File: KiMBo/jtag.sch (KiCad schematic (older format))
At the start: 9 parts, among them U1 OSD3358, Y2 AH-32.768KDZY-T, Y3 7A-24.000MAAJ-T

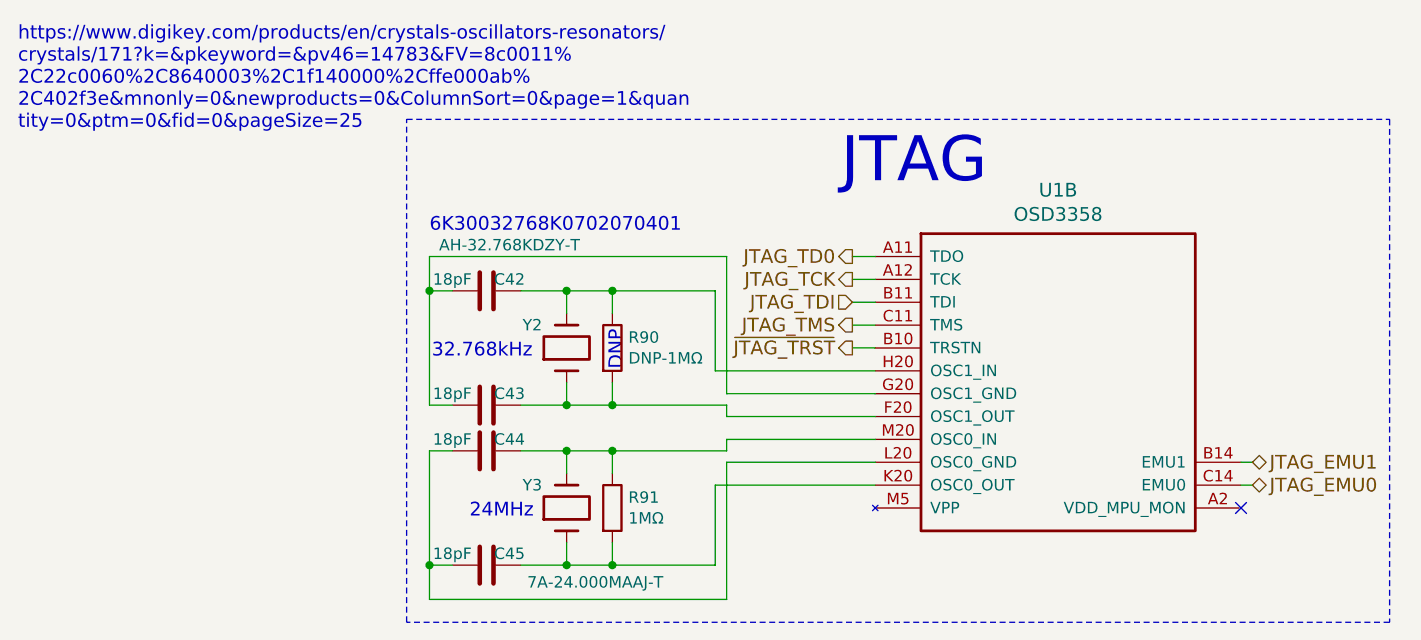
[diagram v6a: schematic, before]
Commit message: Add ferrite beads to the 5V and 3V pins at the SPI connectors
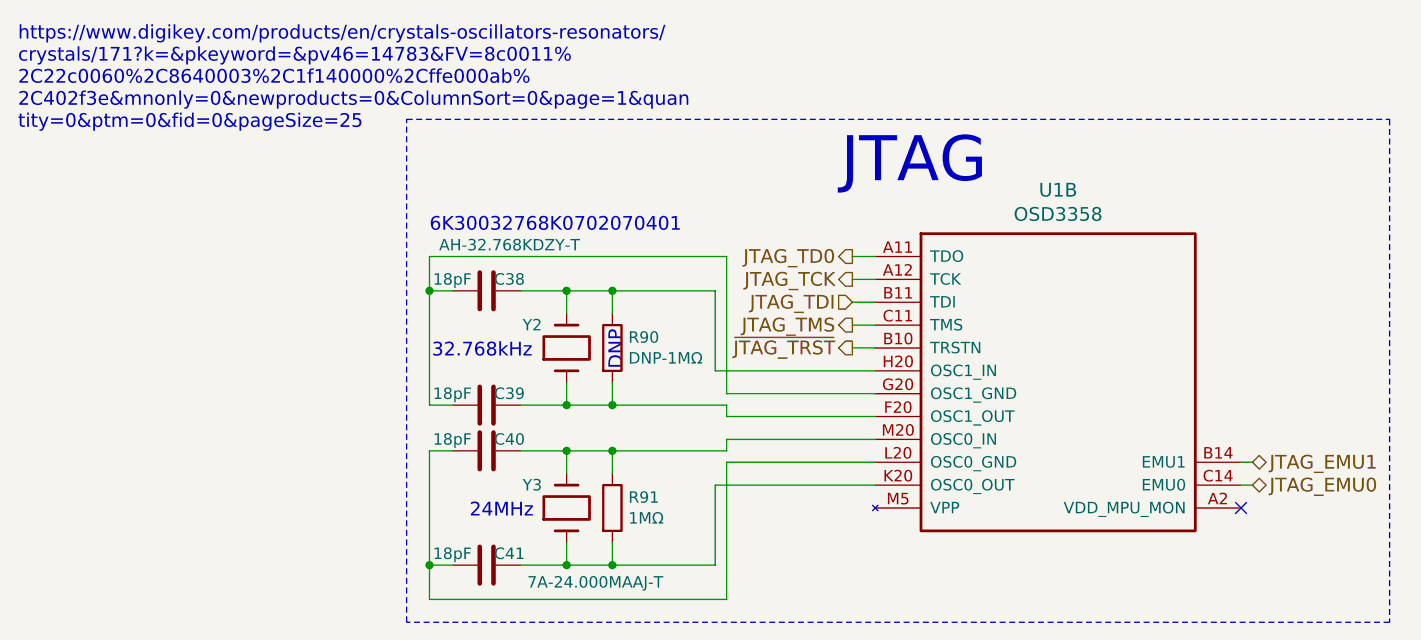
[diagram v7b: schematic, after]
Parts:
- renumbered C42 to C38, C43 to C39, C44 to C40, C45 to C41
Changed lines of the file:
@@
 $EndComp
 $Comp
-L C C44
+L C C40
 U 1 1 589C1D01
 P 4150 3750
-F 0 "C44" V 4200 3850 50  0000 C CNN
+F 0 "C40" V 4200 3850 50  0000 C CNN
 F 1 "18pF" V 4200 3600 50  0000 C CNN
 F 2 "Capacitors_SMD:C_0603" H 4150 3750 50  0001 C CNN
@@
 $EndComp
 $Comp
-L C C45
+L C C41
 U 1 1 589C1D08
 P 4150 4250
-F 0 "C45" V 4200 4350 50  0000 C CNN
+F 0 "C41" V 4200 4350 50  0000 C CNN
 F 1 "18pF" V 4200 4100 50  0000 C CNN
 F 2 "Capacitors_SMD:C_0603" H 4150 4250 50  0001 C CNN
@@
 $EndComp
 $Comp
-L C C43
+L C C39
 U 1 1 589C1D16
 P 4150 3550
-F 0 "C43" V 4200 3650 50  0000 C CNN
+F 0 "C39" V 4200 3650 50  0000 C CNN
 F 1 "18pF" V 4200 3400 50  0000 C CNN
 F 2 "Capacitors_SMD:C_0603" H 4150 3550 50  0001 C CNN
@@
 $EndComp
 $Comp
-L C C42
+L C C38
 U 1 1 589C1D1D
 P 4150 3050
-F 0 "C42" V 4200 3150 50  0000 C CNN
+F 0 "C38" V 4200 3150 50  0000 C CNN
 F 1 "18pF" V 4200 2900 50  0000 C CNN
 F 2 "Capacitors_SMD:C_0603" H 4150 3050 50  0001 C CNN

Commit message: Complete SPI, ADC, and Endstop header layout/position, add zone around the SiP
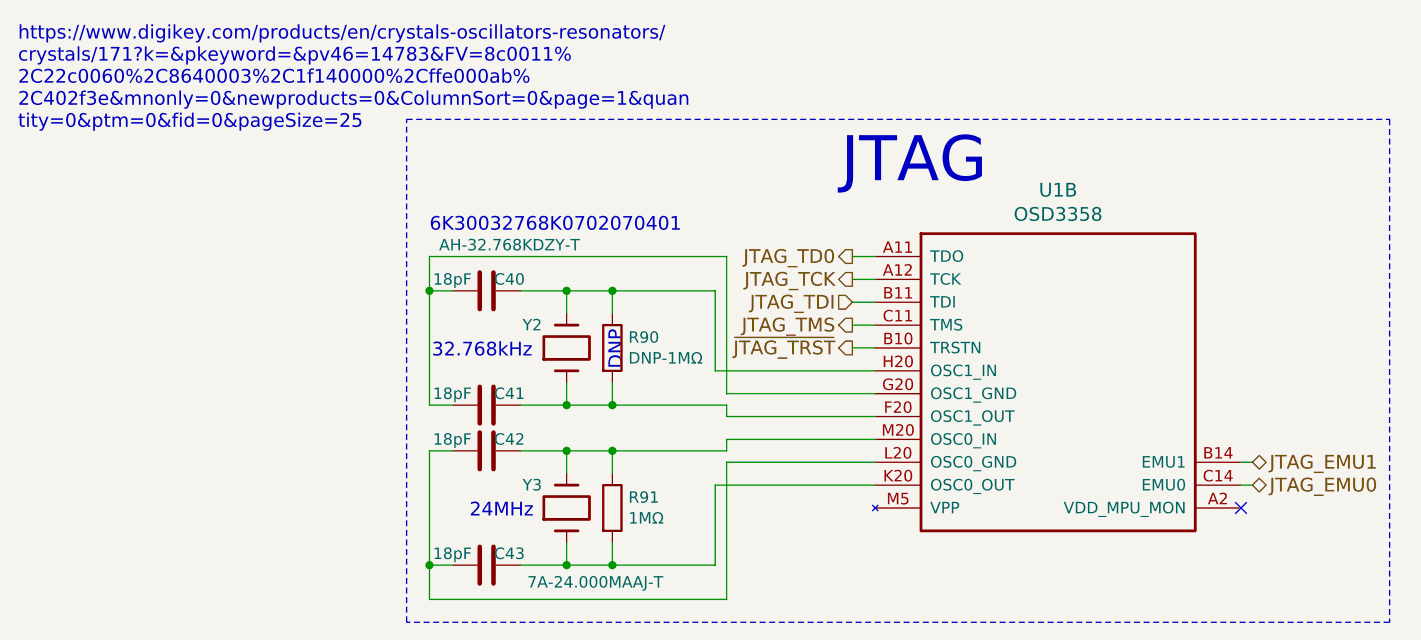
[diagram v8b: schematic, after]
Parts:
- renumbered C38 to C40, C39 to C41, C40 to C42, C41 to C43
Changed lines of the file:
@@
 $EndComp
 $Comp
-L C C40
+L C C42
 U 1 1 589C1D01
 P 4150 3750
-F 0 "C40" V 4200 3850 50  0000 C CNN
+F 0 "C42" V 4200 3850 50  0000 C CNN
 F 1 "18pF" V 4200 3600 50  0000 C CNN
 F 2 "Capacitors_SMD:C_0603" H 4150 3750 50  0001 C CNN
@@
 $EndComp
 $Comp
-L C C41
+L C C43
 U 1 1 589C1D08
 P 4150 4250
-F 0 "C41" V 4200 4350 50  0000 C CNN
+F 0 "C43" V 4200 4350 50  0000 C CNN
 F 1 "18pF" V 4200 4100 50  0000 C CNN
 F 2 "Capacitors_SMD:C_0603" H 4150 4250 50  0001 C CNN
@@
 $EndComp
 $Comp
-L C C39
+L C C41
 U 1 1 589C1D16
 P 4150 3550
-F 0 "C39" V 4200 3650 50  0000 C CNN
+F 0 "C41" V 4200 3650 50  0000 C CNN
 F 1 "18pF" V 4200 3400 50  0000 C CNN
 F 2 "Capacitors_SMD:C_0603" H 4150 3550 50  0001 C CNN
@@
 $EndComp
 $Comp
-L C C38
+L C C40
 U 1 1 589C1D1D
 P 4150 3050
-F 0 "C38" V 4200 3150 50  0000 C CNN
+F 0 "C40" V 4200 3150 50  0000 C CNN
 F 1 "18pF" V 4200 2900 50  0000 C CNN
 F 2 "Capacitors_SMD:C_0603" H 4150 3050 50  0001 C CNN
